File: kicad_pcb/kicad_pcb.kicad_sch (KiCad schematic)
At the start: 17 parts, among them IC1 LM358DR2G, IC2 MCP4725A0T-E_CH, IC3 L78M24ACDT-TR

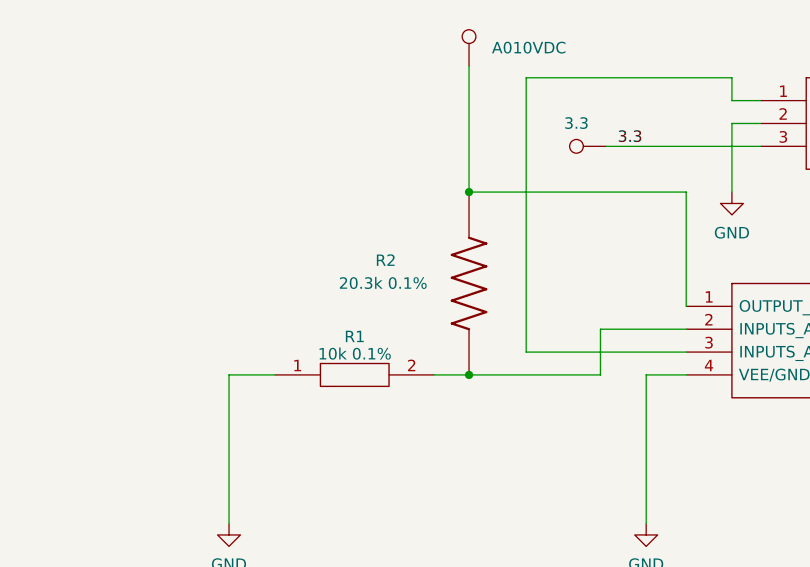
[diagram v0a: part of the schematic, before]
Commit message: 20.3k rsistor update
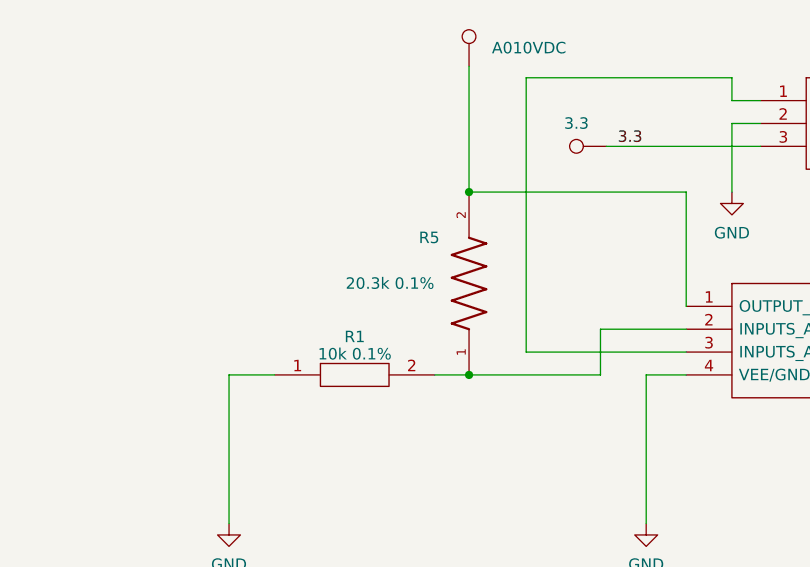
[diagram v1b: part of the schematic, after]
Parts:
- removed R2: 20.3k 0.1%, Resistor_THT:R_Axial_DIN0207_L6.3mm_D2.5mm_P10.16mm_Horizontal, symbol Snapeda:TNPW080520K3BEEN
- added R5: 20.3k 0.1%, Snapeda:TNPW080520K3BEEA_RESC2012X55N, symbol Snapeda:TNPW080520K3BEEA
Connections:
- net at IC1.1 (OUTPUT_A), TP6.1: now also R5.2
- net at IC1.2 (INPUTS_A_1), R1.2: now also R5.1
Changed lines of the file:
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@@
+	)
+	(junction
+		(at 185.42 69.85)
+		(diameter 0)
+		(color 0 0 0 0)
+	)
+	(junction
+		(at 265.43 82.55)
+		(diameter 0)
+		(color 0 0 0 0)
 	)
 	(junction
@@
 	)
 	(junction
-		(at 185.42 69.85)
-		(diameter 0)
-		(color 0 0 0 0)
-	)
-	(junction
-		(at 265.43 82.55)
-		(diameter 0)
-		(color 0 0 0 0)
-	)
-	(junction
 		(at 250.19 72.39)
 		(diameter 0)
@@
 	(wire
 		(pts
+			(xy 181.61 90.17) (xy 185.42 90.17)
+		)
+		(stroke
+			(width 0)
+			(type default)
+		)
+	)
+	(wire
+		(pts
+			(xy 185.42 69.85) (xy 185.42 55.88)
+		)
+		(stroke
+			(width 0)
+			(type default)
+		)
+	)
+	(wire
+		(pts
+			(xy 26.67 62.23) (xy 38.1 62.23)
+		)
+		(stroke
+			(width 0)
+			(type default)
+		)
+	)
+	(wire
+		(pts
+			(xy 38.1 62.23) (xy 38.1 68.58)
+		)
+		(stroke
+			(width 0)
+			(type default)
+		)
+	)
+	(wire
+		(pts
 			(xy 185.42 90.17) (xy 200.025 90.17)
-		)
-		(stroke
-			(width 0)
-			(type default)
-		)
-	)
-	(wire
-		(pts
-			(xy 185.42 69.85) (xy 185.42 55.88)
-		)
-		(stroke
-			(width 0)
-			(type default)
-		)
-	)
-	(wire
-		(pts
-			(xy 181.61 90.17) (xy 185.42 90.17)
-		)
-		(stroke
-			(width 0)
-			(type default)
-		)
-	)
-	(wire
-		(pts
-			(xy 26.67 62.23) (xy 38.1 62.23)
-		)
-		(stroke
-			(width 0)
-			(type default)
-		)
-	)
-	(wire
-		(pts
-			(xy 38.1 62.23) (xy 38.1 68.58)
 		)
 		(stroke
@@
 	)
 	(symbol
-		(lib_id "Snapeda:TNPW080520K3BEEN")
-		(at 185.42 80.01 90)
-		(unit 1)
-		(exclude_from_sim no)
-		(in_bom yes)
-		(on_board yes)
-		(dnp no)
-		(property "Reference" "R2"
-			(at 175.006 77.47 90)
-			(effects
-				(font
-					(size 1.27 1.27)
-				)
-				(justify right)
-			)
-		)
-		(property "Value" "20.3k 0.1%"
-			(at 170.942 80.01 90)
-			(effects
-				(font
-					(size 1.27 1.27)
-				)
-				(justify right)
-			)
-		)
-		(property "Footprint" "Resistor_THT:R_Axial_DIN0207_L6.3mm_D2.5mm_P10.16mm_Horizontal"
-			(at 185.42 80.01 0)
-			(effects
-				(font
-					(size 1.27 1.27)
-				)
-				(justify left bottom)
-				(hide yes)
-			)
-		)
-		(property "Datasheet" ""
-			(at 185.42 80.01 0)
-			(effects
-				(font
-					(size 1.27 1.27)
-				)
-				(justify left bottom)
-				(hide yes)
-			)
-		)
-		(property "Description" ""
-			(at 185.42 80.01 0)
-			(effects
-				(font
-					(size 1.27 1.27)
-				)
-				(hide yes)
-			)
-		)
-		(property "Manufacturer_Part_Number" "TNPW060320K3BEEA"
-			(at 185.42 80.01 90)
-			(effects
-				(font
-					(size 1.27 1.27)
-				)
-				(hide yes)
-			)
-		)
-		(pin "1"
-		)
-		(pin "2"
-		)
-		(instances
-			(project "kicad_pcb"
-				(path "/9ecf7fa2-a852-4268-b56d-a929f388cbe9"
-					(reference "R2")
-					(unit 1)
-				)
-			)
-		)
-	)
-	(symbol
 		(lib_id "Connector:TestPoint")
 		(at 26.67 87.63 90)
@@
 					(unit 1)
 				)
+			)
+		)
+	)
+	(symbol
+		(lib_id "Snapeda:TNPW080520K3BEEA")
+		(at 185.42 80.01 90)
+		(unit 1)
+		(exclude_from_sim no)
+		(in_bom yes)
+		(on_board yes)
+		(dnp no)
+		(property "Reference" "R5"
+			(at 179.832 74.93 90)
+			(effects
+				(font
+					(size 1.27 1.27)
+				)
+				(justify right)
+			)
+		)
+		(property "Value" "20.3k 0.1%"
+			(at 171.704 80.01 90)
+			(effects
+				(font
+					(size 1.27 1.27)
+				)
+				(justify right)
+			)
+		)
+		(property "Footprint" "Snapeda:TNPW080520K3BEEA_RESC2012X55N"
+			(at 185.42 80.01 0)
+			(effects
+				(font
+					(size 1.27 1.27)
+				)
+				(justify bottom)
+				(hide yes)
+			)
+		)
+		(property "Datasheet" ""
+			(at 185.42 80.01 0)
+			(effects
+				(font
+					(size 1.27 1.27)
+				)
+				(hide yes)
+			)
+		)
+		(property "Description" ""
+			(at 185.42 80.01 0)
+			(effects
+				(font
+					(size 1.27 1.27)
+				)
+				(hide yes)
+			)
+		)
+		(property "MF" "Vishay Dale"
+			(at 185.42 80.01 0)
+			(effects
+				(font
+					(size 1.27 1.27)
+				)
+				(justify bottom)
+				(hide yes)
+			)
+		)
+		(property "Description_1" "\n20.3 kOhms ±0.1% 0.26W Chip Resistor 0805 (2012 Metric) Anti-Sulfur, Automotive AEC-Q200, Moisture Resistant Thin Film\n"
+			(at 185.42 80.01 0)
+			(effects
+				(font
+					(size 1.27 1.27)
+				)
+				(justify bottom)
+				(hide yes)
+			)
+		)
+		(property "Package" "2012 Vishay"
+			(at 185.42 80.01 0)
+			(effects
+				(font
+					(size 1.27 1.27)
+				)
+				(justify bottom)
+				(hide yes)
+			)
+		)
+		(property "Price" "None"
+			(at 185.42 80.01 0)
+			(effects
+				(font
+					(size 1.27 1.27)
+				)
+				(justify bottom)
+				(hide yes)
+			)
+		)
+		(property "SnapEDA_Link" "https://www.snapeda.com/parts/TNPW080520K3BEEA/Vishay+Dale/view-part/?ref=snap"
+			(at 185.42 80.01 0)
+			(effects
+				(font
+					(size 1.27 1.27)
+				)
+				(justify bottom)
+				(hide yes)
+			)
+		)
+		(property "MP" "TNPW080520K3BEEA"
+			(at 185.42 80.01 0)
+			(effects
+				(font
+					(size 1.27 1.27)
+				)
+				(justify bottom)
+				(hide yes)
+			)
+		)
+		(property "Availability" "In Stock"
+			(at 185.42 80.01 0)
+			(effects
+				(font
+					(size 1.27 1.27)
+				)
+				(justify bottom)
+				(hide yes)
+			)
+		)
+		(property "Check_prices" "https://www.snapeda.com/parts/TNPW080520K3BEEA/Vishay+Dale/view-part/?ref=eda"
+			(at 185.42 80.01 0)
+			(effects
+				(font
+					(size 1.27 1.27)
+				)
+				(justify bottom)
+				(hide yes)
+			)
+		)
+		(pin "2"
+		)
+		(pin "1"
+		)
+		(instances
+			(project "kicad_pcb"
+				(path "/9ecf7fa2-a852-4268-b56d-a929f388cbe9"
+					(reference "R5")
+					(unit 1)
+				)

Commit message: 20.3k resistor update to KOA
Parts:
- R5: footprint Snapeda:TNPW080520K3BEEA_RESC2012X55N -> Snapeda:RN73H1JTTD2032B25_RESC1608X55N; symbol Snapeda:TNPW080520K3BEEA -> Snapeda:RN73H1JTTD2032B25; Check_prices https://www.snapeda.com/parts/TNPW080520K3BEEA/Vishay+Dale/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 -> https://www.snapeda.com/parts/RN73H1JTTD2032B25/KOA+Speer/v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; Description_1 20.3 kOhms ±0.1% 0.26W Chip Resistor 0805 (2012 Metric) Ant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 -> 20.3 kOhms ±0.1% 0.1W, 1/10W Chip Resistor 0603 (1608 Metri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; MF Vishay Dale -> KOA Speer; MP TNPW080520K3BEEA -> RN73H1JTTD2032B25; Package 2012 Vishay -> 603 KOA; SnapEDA_Link https://www.snapeda.com/parts/TNPW080520K3BEEA/Vishay+Dale/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 -> https://www.snapeda.com/parts/RN73H1JTTD2032B25/KOA+Speer/v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
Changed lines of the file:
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@@
 	)
 	(symbol
-		(lib_id "Snapeda:TNPW080520K3BEEA")
+		(lib_id "Snapeda:RN73H1JTTD2032B25")
 		(at 185.42 80.01 90)
 		(unit 1)
@@
 			)
 		)
-		(property "Footprint" "Snapeda:TNPW080520K3BEEA_RESC2012X55N"
+		(property "Footprint" "Snapeda:RN73H1JTTD2032B25_RESC1608X55N"
 			(at 185.42 80.01 0)
 			(effects
@@
 			)
 		)
-		(property "MF" "Vishay Dale"
+		(property "MF" "KOA Speer"
 			(at 185.42 80.01 0)
 			(effects
@@
 			)
 		)
-		(property "Description_1" "\n20.3 kOhms ±0.1% 0.26W Chip Resistor 0805 (2012 Metric) Anti-Sulfur, Automotive AEC-Q200, Moisture Resistant Thin Film\n"
+		(property "Description_1" "\n20.3 kOhms ±0.1% 0.1W, 1/10W Chip Resistor 0603 (1608 Metric) Automotive AEC-Q200, Moisture Resistant Metal Film\n"
 			(at 185.42 80.01 0)
 			(effects
@@
 			)
 		)
-		(property "Package" "2012 Vishay"
+		(property "Package" "603 KOA"
 			(at 185.42 80.01 0)
 			(effects
@@
 			)
 		)
-		(property "SnapEDA_Link" "https://www.snapeda.com/parts/TNPW080520K3BEEA/Vishay+Dale/view-part/?ref=snap"
+		(property "SnapEDA_Link" "https://www.snapeda.com/parts/RN73H1JTTD2032B25/KOA+Speer/view-part/?ref=snap"
 			(at 185.42 80.01 0)
 			(effects
@@
 			)
 		)
-		(property "MP" "TNPW080520K3BEEA"
+		(property "MP" "RN73H1JTTD2032B25"
 			(at 185.42 80.01 0)
 			(effects
@@
 			)
 		)
-		(property "Check_prices" "https://www.snapeda.com/parts/TNPW080520K3BEEA/Vishay+Dale/view-part/?ref=eda"
+		(property "Check_prices" "https://www.snapeda.com/parts/RN73H1JTTD2032B25/KOA+Speer/view-part/?ref=eda"
 			(at 185.42 80.01 0)
 			(effects
